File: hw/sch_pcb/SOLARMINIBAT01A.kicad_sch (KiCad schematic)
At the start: 4 parts

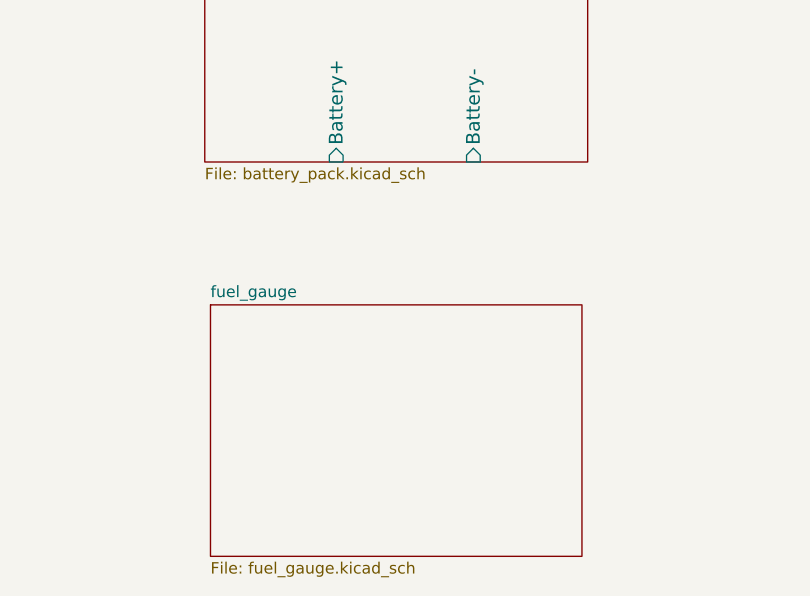
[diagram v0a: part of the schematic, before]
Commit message: cleanup unused file.
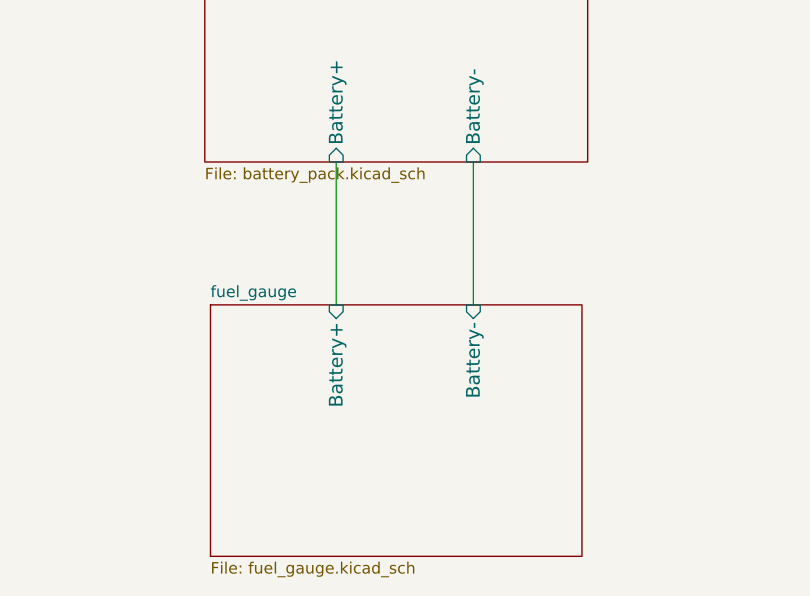
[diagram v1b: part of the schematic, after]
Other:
- sheet fuel_gauge ports: added Battery+, Battery-; removed none
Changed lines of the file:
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@@
   (no_connect (at 243.205 22.86))
   (no_connect (at 253.365 22.86))
+  (wire (pts (xy 129.54 89.535) (xy 129.54 105.41))
+    (stroke (width 0) (type default) (color 0 0 0 0))
+  )
+  (wire (pts (xy 114.3 89.535) (xy 114.3 105.41))
+    (stroke (width 0) (type default) (color 0 0 0 0))
+  )
   (symbol (lib_id "MLAB_MECHANICAL:HOLE") (at 243.205 21.59 270) (unit 1)
     (in_bom yes) (on_board yes) (fields_autoplaced)
@@
       (effects (font (size 1.27 1.27)) (justify left top))
     )
+    (pin "Battery-" input (at 129.54 105.41 90)
+      (effects (font (size 1.524 1.524)) (justify right))
+    )
+    (pin "Battery+" input (at 114.3 105.41 90)
+      (effects (font (size 1.524 1.524)) (justify right))
+    )
   )
   (sheet_instances
@@
       (reference "#PWR?") (unit 1) (value "GND") (footprint "")
     )
-    (path "/aabf0346-8f10-4bb0-86f6-0ff8e72d6db1/4ebcb038-ed6f-418f-b723-8d00834831bd"
+    (path "/aabf0346-8f10-4bb0-86f6-0ff8e72d6db1/62df70fb-4e53-4c17-8714-768cf1e1515d"
       (reference "#PWR?") (unit 1) (value "GND") (footprint "")
     )
@@
     (path "/6044c252-cae8-4c38-b9d6-66858f0fde85/9b2144e5-e150-4e36-8dd0-57044a8430ca"
       (reference "#PWR?") (unit 1) (value "GND") (footprint "")
+    )
+    (path "/aabf0346-8f10-4bb0-86f6-0ff8e72d6db1/abba4e23-d87a-40b0-af85-0dd431cce3cf"
+      (reference "#PWR?") (unit 1) (value "+3.3V") (footprint "")
     )
     (path "/aabf0346-8f10-4bb0-86f6-0ff8e72d6db1/b5160f60-99a6-4a11-81ca-7fbd8c16f063"
@@
       (reference "#PWR?") (unit 1) (value "GND") (footprint "")
     )
+    (path "/aabf0346-8f10-4bb0-86f6-0ff8e72d6db1/c622d264-9ce6-4134-9dc7-1b35c55869d0"
+      (reference "#PWR?") (unit 1) (value "+3.3V") (footprint "")
+    )
     (path "/6044c252-cae8-4c38-b9d6-66858f0fde85/d66225d6-89ff-4507-a881-52e05f4653d6"
       (reference "#PWR?") (unit 1) (value "GND") (footprint "")
@@
       (reference "D?") (unit 1) (value "ORAGE") (footprint "Mlab_D:LED_1206")
     )
-    (path "/aabf0346-8f10-4bb0-86f6-0ff8e72d6db1/203c39d5-3245-4502-8b8e-5d04d2ce68cf"
-      (reference "J?") (unit 1) (value "JUMP_2x1") (footprint "Mlab_Pin_Headers:Straight_1x02")
-    )
-    (path "/aabf0346-8f10-4bb0-86f6-0ff8e72d6db1/5082e2ca-7df8-48ae-a1b0-8847ed874b82"
-      (reference "J?") (unit 1) (value "JUMP_2x1") (footprint "Mlab_Pin_Headers:Straight_1x02")
-    )
-    (path "/aabf0346-8f10-4bb0-86f6-0ff8e72d6db1/50e8f211-a19b-4d6f-a7b8-00aec520100e"
-      (reference "J?") (unit 1) (value "JUMP_2x1") (footprint "Mlab_Pin_Headers:Straight_1x02")
-    )
     (path "/6044c252-cae8-4c38-b9d6-66858f0fde85/5d8562eb-d038-4182-83e5-3d540ae1b907"
       (reference "J?") (unit 1) (value "WAGO 256 BLUE") (footprint "Mlab_CON:WAGO256")
@@
       (reference "J?") (unit 1) (value "HEADER_1x01") (footprint "Mlab_Pin_Headers:Straight_1x01")
     )
-    (path "/aabf0346-8f10-4bb0-86f6-0ff8e72d6db1/da59c663-037a-4c14-98ec-72a07b2de130"
-      (reference "J?") (unit 1) (value "JUMP_2x1") (footprint "Mlab_Pin_Headers:Straight_1x02")
-    )
     (path "/6044c252-cae8-4c38-b9d6-66858f0fde85/faf597ca-e145-472d-8b8e-fd99f24dc91f"
       (reference "L?") (unit 1) (value "10uH - DE1205-10") (footprint "Mlab_L:DE1205-10")
@@
       (reference "M?") (unit 1) (value "HOLE") (footprint "Mlab_Mechanical:MountingHole_3mm")
     )
+    (path "/aabf0346-8f10-4bb0-86f6-0ff8e72d6db1/a784774c-c917-4510-97a6-fef1071a76f3"
+      (reference "P?") (unit 1) (value "HEADER_2x05_PARALLEL") (footprint "Mlab_Pin_Headers:Straight_2x05")
+    )
     (path "/6044c252-cae8-4c38-b9d6-66858f0fde85/13dbe897-417b-43d0-a751-d9a5fbcdfe5e"

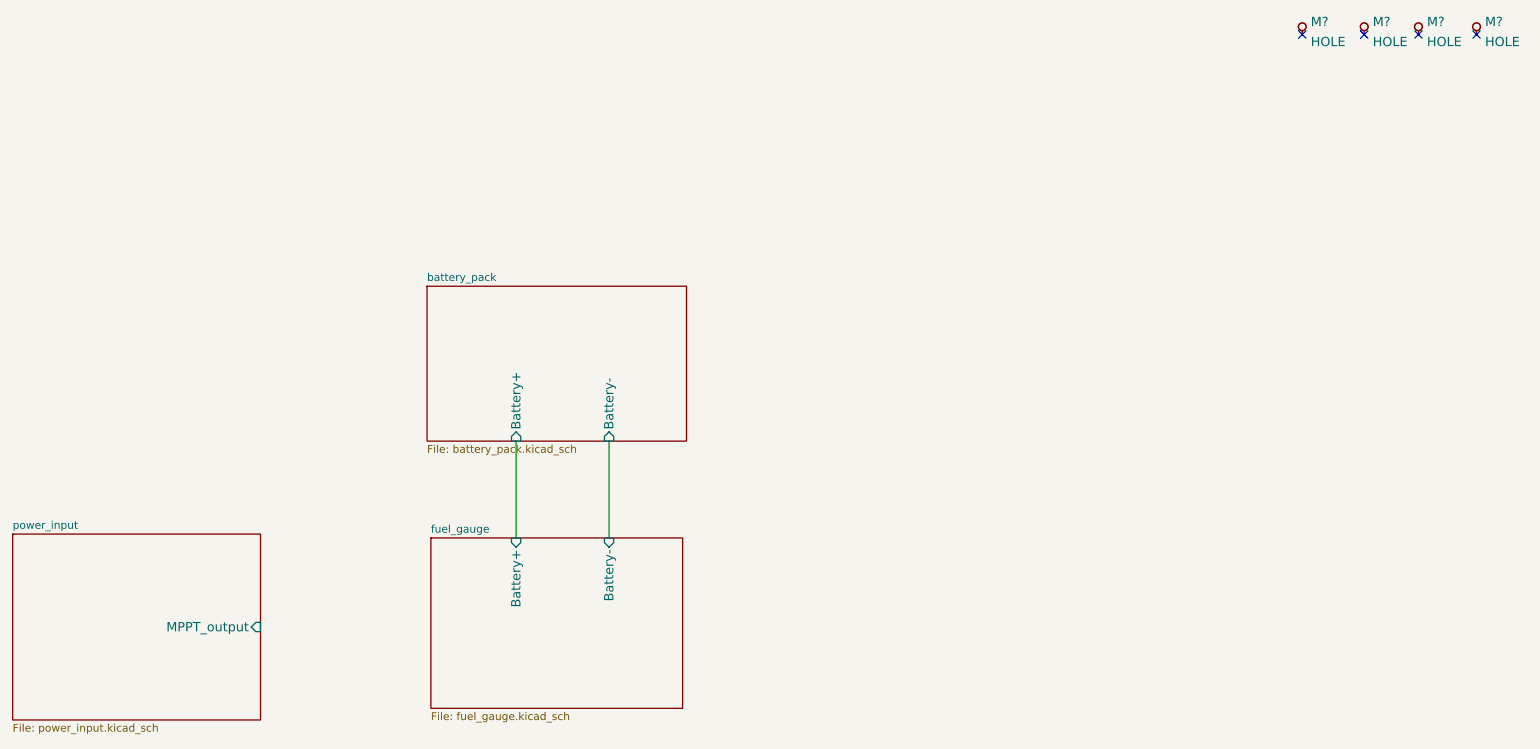
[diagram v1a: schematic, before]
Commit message: finish gauge schematics design.
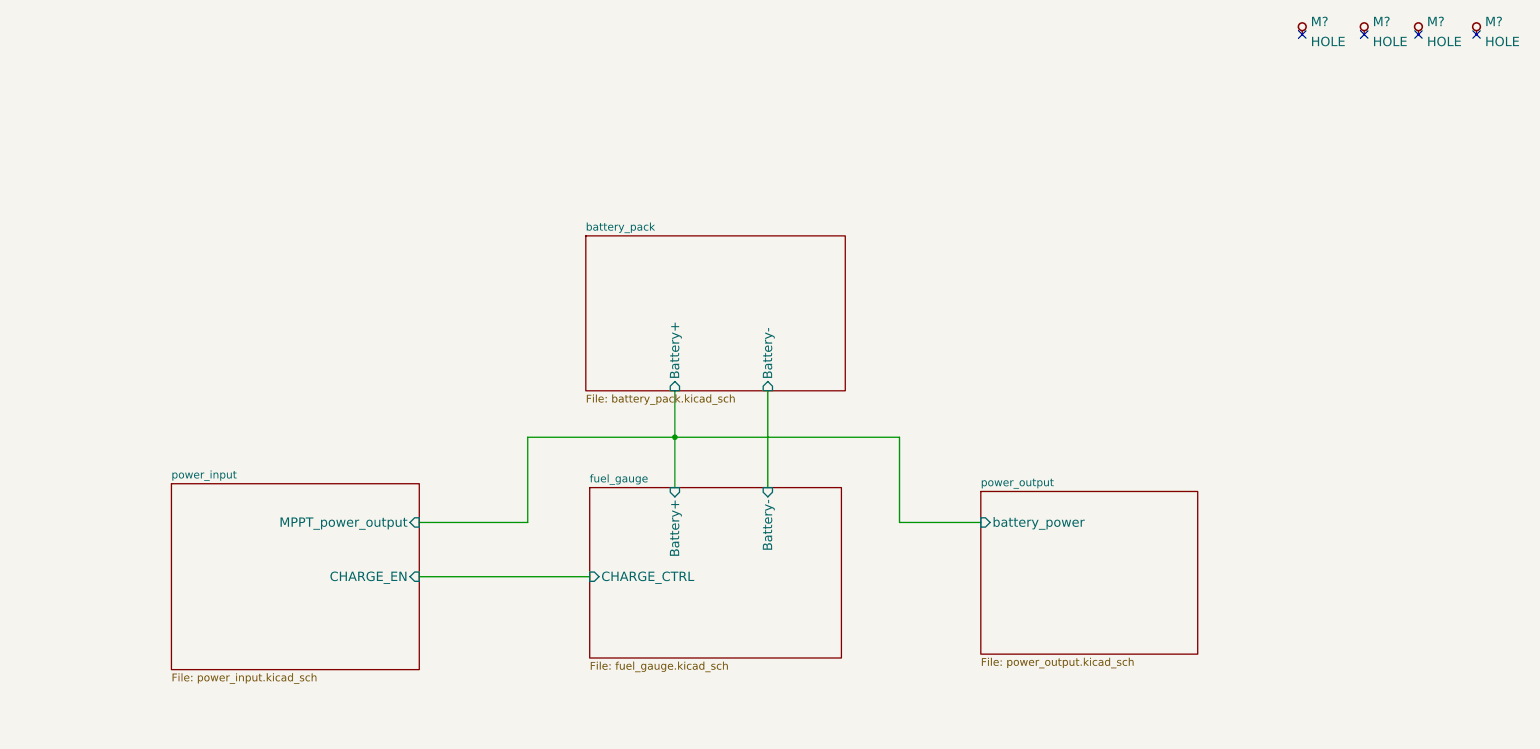
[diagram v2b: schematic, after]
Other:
- added sheet power_output (power_output.kicad_sch)
- sheet fuel_gauge ports: added CHARGE_CTRL; removed none
- sheet power_input ports: added CHARGE_EN, MPPT_power_output; removed MPPT_output
- company: jacho <jacho@mlab.cz> -> MLAB.cz
- title: LION2CELL01D -> SOLARMINIBAT01A
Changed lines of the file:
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@@
   (paper "A4")
   (title_block
-    (title "LION2CELL01D")
-    (date "2021-06-02")
-    (rev "D")
-    (company "jacho <jacho@mlab.cz>")
-    (comment 2 "2-cell Li-ion Battery Managment System")
+    (title "SOLARMINIBAT01A")
+    (date "2022-07-20")
+    (rev "A")
+    (company "MLAB.cz")
+    (comment 2 "Solar charged LTO Battery Managment System")
+  )
+  (junction (at 140.335 88.9) (diameter 0) (color 0 0 0 0)
   )
   (no_connect (at 262.255 22.86))
@@
   (no_connect (at 243.205 22.86))
   (no_connect (at 253.365 22.86))
-  (wire (pts (xy 129.54 89.535) (xy 129.54 105.41))
-    (stroke (width 0) (type default) (color 0 0 0 0))
-  )
-  (wire (pts (xy 114.3 89.535) (xy 114.3 105.41))
+  (wire (pts (xy 177.165 102.87) (xy 190.5 102.87))
+    (stroke (width 0) (type default) (color 0 0 0 0))
+  )
+  (wire (pts (xy 116.205 102.87) (xy 116.205 88.9))
+    (stroke (width 0) (type default) (color 0 0 0 0))
+  )
+  (wire (pts (xy 98.425 102.87) (xy 116.205 102.87))
+    (stroke (width 0) (type default) (color 0 0 0 0))
+  )
+  (wire (pts (xy 155.575 81.28) (xy 155.575 97.155))
+    (stroke (width 0) (type default) (color 0 0 0 0))
+  )
+  (wire (pts (xy 140.335 88.9) (xy 140.335 97.155))
+    (stroke (width 0) (type default) (color 0 0 0 0))
+  )
+  (wire (pts (xy 140.335 88.9) (xy 177.165 88.9))
+    (stroke (width 0) (type default) (color 0 0 0 0))
+  )
+  (wire (pts (xy 116.205 88.9) (xy 140.335 88.9))
+    (stroke (width 0) (type default) (color 0 0 0 0))
+  )
+  (wire (pts (xy 98.425 111.76) (xy 126.365 111.76))
+    (stroke (width 0) (type default) (color 0 0 0 0))
+  )
+  (wire (pts (xy 177.165 88.9) (xy 177.165 102.87))
+    (stroke (width 0) (type default) (color 0 0 0 0))
+  )
+  (wire (pts (xy 140.335 81.28) (xy 140.335 88.9))
     (stroke (width 0) (type default) (color 0 0 0 0))
   )
@@
     (pin "1")
   )
-  (sheet (at 99.695 64.135) (size 42.545 25.4) (fields_autoplaced)
+  (sheet (at 125.73 55.88) (size 42.545 25.4) (fields_autoplaced)
     (stroke (width 0.1524) (type solid) (color 0 0 0 0))
     (fill (color 0 0 0 0.0000))
-    (property "Sheet name" "battery_pack" (id 0) (at 99.695 63.4234 0)
+    (property "Sheet name" "battery_pack" (id 0) (at 125.73 55.1684 0)
       (effects (font (size 1.27 1.27)) (justify left bottom))
     )
-    (property "Sheet file" "battery_pack.kicad_sch" (id 1) (at 99.695 90.1196 0)
+    (property "Sheet file" "battery_pack.kicad_sch" (id 1) (at 125.73 81.8646 0)
       (effects (font (size 1.27 1.27)) (justify left top))
     )
-    (pin "Battery+" input (at 114.3 89.535 270)
-      (effects (font (size 1.524 1.524)) (justify left))
-    )
-    (pin "Battery-" input (at 129.54 89.535 270)
-      (effects (font (size 1.524 1.524)) (justify left))
-    )
-  )
-  (sheet (at 31.75 104.775) (size 40.64 30.48) (fields_autoplaced)
+    (pin "Battery+" input (at 140.335 81.28 270)
+      (effects (font (size 1.524 1.524)) (justify left))
+    )
+    (pin "Battery-" input (at 155.575 81.28 270)
+      (effects (font (size 1.524 1.524)) (justify left))
+    )
+  )
+  (sheet (at 57.785 96.52) (size 40.64 30.48) (fields_autoplaced)
     (stroke (width 0.1524) (type solid) (color 0 0 0 0))
     (fill (color 0 0 0 0.0000))
-    (property "Sheet name" "power_input" (id 0) (at 31.75 104.0634 0)
+    (property "Sheet name" "power_input" (id 0) (at 57.785 95.8084 0)
       (effects (font (size 1.27 1.27)) (justify left bottom))
     )
-    (property "Sheet file" "power_input.kicad_sch" (id 1) (at 31.75 135.8396 0)
+    (property "Sheet file" "power_input.kicad_sch" (id 1) (at 57.785 127.5846 0)
       (effects (font (size 1.27 1.27)) (justify left top))
     )
-    (pin "MPPT_output" input (at 72.39 120.015 0)
+    (pin "MPPT_power_output" input (at 98.425 102.87 0)
       (effects (font (size 1.524 1.524)) (justify right))
     )
-  )
-  (sheet (at 100.33 105.41) (size 41.275 27.94) (fields_autoplaced)
+    (pin "CHARGE_EN" input (at 98.425 111.76 0)
+      (effects (font (size 1.524 1.524)) (justify right))
+    )
+  )
+  (sheet (at 126.365 97.155) (size 41.275 27.94) (fields_autoplaced)
     (stroke (width 0.1524) (type solid) (color 0 0 0 0))
     (fill (color 0 0 0 0.0000))
-    (property "Sheet name" "fuel_gauge" (id 0) (at 100.33 104.6984 0)
+    (property "Sheet name" "fuel_gauge" (id 0) (at 126.365 96.4434 0)
       (effects (font (size 1.27 1.27)) (justify left bottom))
     )
-    (property "Sheet file" "fuel_gauge.kicad_sch" (id 1) (at 100.33 133.9346 0)
+    (property "Sheet file" "fuel_gauge.kicad_sch" (id 1) (at 126.365 125.6796 0)
       (effects (font (size 1.27 1.27)) (justify left top))
     )
-    (pin "Battery-" input (at 129.54 105.41 90)
+    (pin "Battery-" input (at 155.575 97.155 90)
       (effects (font (size 1.524 1.524)) (justify right))
     )
-    (pin "Battery+" input (at 114.3 105.41 90)
+    (pin "Battery+" input (at 140.335 97.155 90)
       (effects (font (size 1.524 1.524)) (justify right))
+    )
+    (pin "CHARGE_CTRL" input (at 126.365 111.76 180)
+      (effects (font (size 1.524 1.524)) (justify left))
+    )
+  )
+  (sheet (at 190.5 97.79) (size 35.56 26.67) (fields_autoplaced)
+    (stroke (width 0.1524) (type solid) (color 0 0 0 0))
+    (fill (color 0 0 0 0.0000))
+    (property "Sheet name" "power_output" (id 0) (at 190.5 97.0784 0)
+      (effects (font (size 1.27 1.27)) (justify left bottom))
+    )
+    (property "Sheet file" "power_output.kicad_sch" (id 1) (at 190.5 125.0446 0)
+      (effects (font (size 1.27 1.27)) (justify left top))
+    )
+    (pin "battery_power" input (at 190.5 102.87 180)
+      (effects (font (size 1.524 1.524)) (justify left))
     )
   )
@@
     (path "/57fea48e-5c3e-4f84-80e7-cf0f4aa7b3fd" (page "3"))
     (path "/6044c252-cae8-4c38-b9d6-66858f0fde85" (page "4"))
+    (path "/e5c56c21-dab7-496c-84fa-c1ab8ff603a2" (page "5"))
   )
   (symbol_instances
@@
       (reference "#PWR?") (unit 1) (value "GND") (footprint "")
     )
+    (path "/aabf0346-8f10-4bb0-86f6-0ff8e72d6db1/2b99e94a-0533-4e55-80a1-07cf71906af5"
+      (reference "#PWR?") (unit 1) (value "+3.3V") (footprint "")
+    )
+    (path "/aabf0346-8f10-4bb0-86f6-0ff8e72d6db1/2ec849d6-2130-4700-b059-678de3f84dfc"
+      (reference "#PWR?") (unit 1) (value "+3.3V") (footprint "")
+    )
     (path "/6044c252-cae8-4c38-b9d6-66858f0fde85/4b1ffe94-c14f-477d-8960-b28d2c283902"
       (reference "#PWR?") (unit 1) (value "GND") (footprint "")
@@
       (reference "#PWR?") (unit 1) (value "GND") (footprint "")
     )
+    (path "/e5c56c21-dab7-496c-84fa-c1ab8ff603a2/8978ecad-f5ee-49cb-83ae-4d2492251aba"
+      (reference "#PWR?") (unit 1) (value "+3.3V") (footprint "")
+    )
     (path "/6044c252-cae8-4c38-b9d6-66858f0fde85/8ba42678-755d-49ac-aa0e-9ea5bc3549c2"
-      (reference "#PWR?") (unit 1) (value "GND") (footprint "")
-    )
-    (path "/6044c252-cae8-4c38-b9d6-66858f0fde85/8d96b861-afce-49f9-97b8-556a03399326"
       (reference "#PWR?") (unit 1) (value "GND") (footprint "")
     )
@@
       (reference "P?") (unit 1) (value "HEADER_2x05_PARALLEL") (footprint "Mlab_Pin_Headers:Straight_2x05")
     )
-    (path "/6044c252-cae8-4c38-b9d6-66858f0fde85/13dbe897-417b-43d0-a751-d9a5fbcdfe5e"
-      (reference "R?") (unit 1) (value "-") (footprint "Resistor_SMD:R_0805_2012Metric")
-    )
     (path "/aabf0346-8f10-4bb0-86f6-0ff8e72d6db1/1c5c8c3b-2379-46bb-82c7-dac92b753f7f"
       (reference "R?") (unit 1) (value "100R") (footprint "Mlab_R:SMD-0805")
@@
     )
     (path "/6044c252-cae8-4c38-b9d6-66858f0fde85/9d712681-746a-4a3d-8977-eaa179e202d9"
-      (reference "R?") (unit 1) (value "0R") (footprint "Resistor_SMD:R_0805_2012Metric")
+      (reference "R?") (unit 1) (value "1k") (footprint "Resistor_SMD:R_0805_2012Metric")
     )
     (path "/aabf0346-8f10-4bb0-86f6-0ff8e72d6db1/b075bb3d-7c5c-4df8-b663-3672243e2821"
@@
       (reference "R?") (unit 1) (value "2K2") (footprint "Mlab_R:SMD-0805")
     )
+    (path "/aabf0346-8f10-4bb0-86f6-0ff8e72d6db1/f54588e6-e880-4170-84cc-ca29435aa37f"
+      (reference "R?") (unit 1) (value "1k") (footprint "Mlab_R:SMD-0805")
+    )
     (path "/aabf0346-8f10-4bb0-86f6-0ff8e72d6db1/b25b8dca-42e9-4b4d-950d-68936c26f40e"

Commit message: Edit schema
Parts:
- gave numbers to parts that had none: 4

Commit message: Edit PCB
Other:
- sheet battery_pack ports: added NTC1, NTC2; removed none
- sheet fuel_gauge ports: added NTC1, NTC2; removed none
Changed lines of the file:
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@@
+    (stroke (width 0) (type default) (color 0 0 0 0))
+  )
+  (wire (pts (xy 160.655 81.28) (xy 160.655 97.155))
     (stroke (width 0) (type default) (color 0 0 0 0))
   )
@@
   )
   (wire (pts (xy 155.575 81.28) (xy 155.575 97.155))
+    (stroke (width 0) (type default) (color 0 0 0 0))
+  )
+  (wire (pts (xy 164.465 81.28) (xy 164.465 97.155))
     (stroke (width 0) (type default) (color 0 0 0 0))
   )
@@
       (effects (font (size 1.524 1.524)) (justify left))
     )
+    (pin "NTC1" input (at 160.655 81.28 270)
+      (effects (font (size 1.524 1.524)) (justify left))
+    )
+    (pin "NTC2" input (at 164.465 81.28 270)
+      (effects (font (size 1.524 1.524)) (justify left))
+    )
   )
   (sheet (at 57.785 96.52) (size 40.64 30.48) (fields_autoplaced)
@@
       (effects (font (size 1.524 1.524)) (justify left))
     )
+    (pin "NTC1" input (at 160.655 97.155 90)
+      (effects (font (size 1.524 1.524)) (justify right))
+    )
+    (pin "NTC2" input (at 164.465 97.155 90)
+      (effects (font (size 1.524 1.524)) (justify right))
+    )
   )
